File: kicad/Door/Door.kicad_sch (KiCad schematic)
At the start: 14 parts, among them Q1 Q_NMOS_GDS, Q2 Q_PMOS_GSD, SW1 SW_Push, SW2 USB/BAT, SW3 RST_BTN, U1 NODEMCU v3

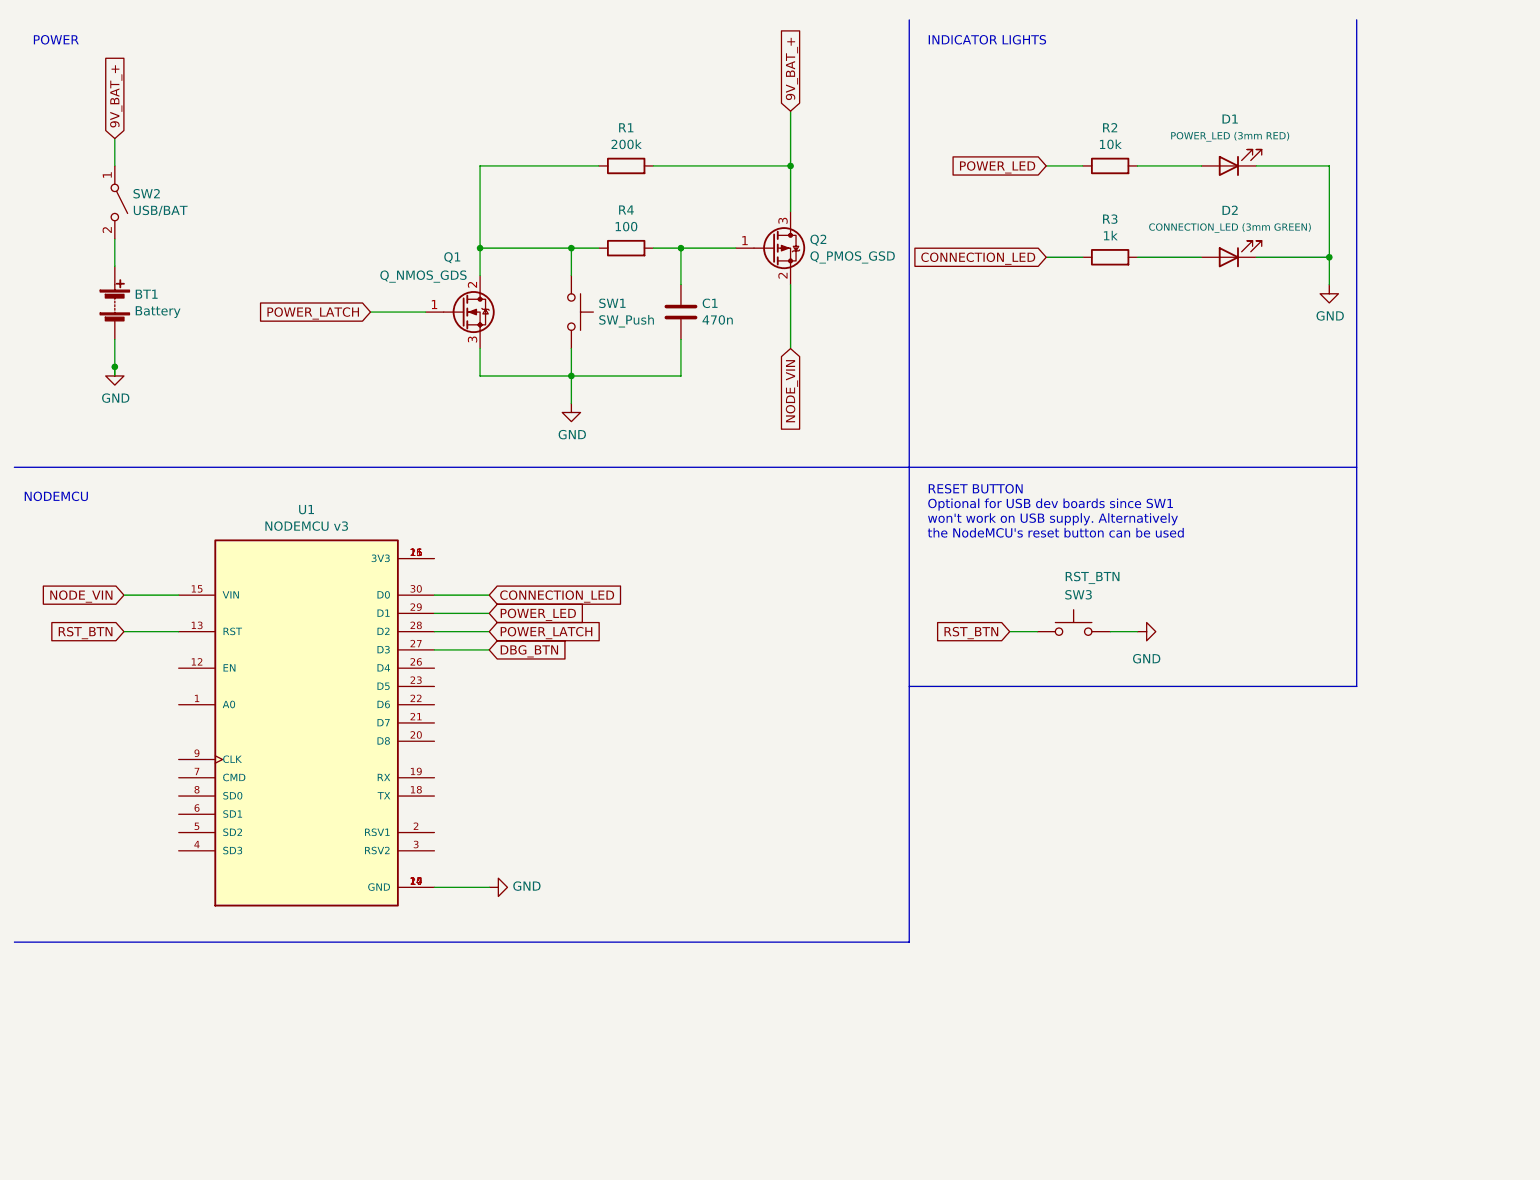
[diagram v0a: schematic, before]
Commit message: README: Added images
Signed-off-by: Patrick Pedersen <ctx.xda@gmail.com>
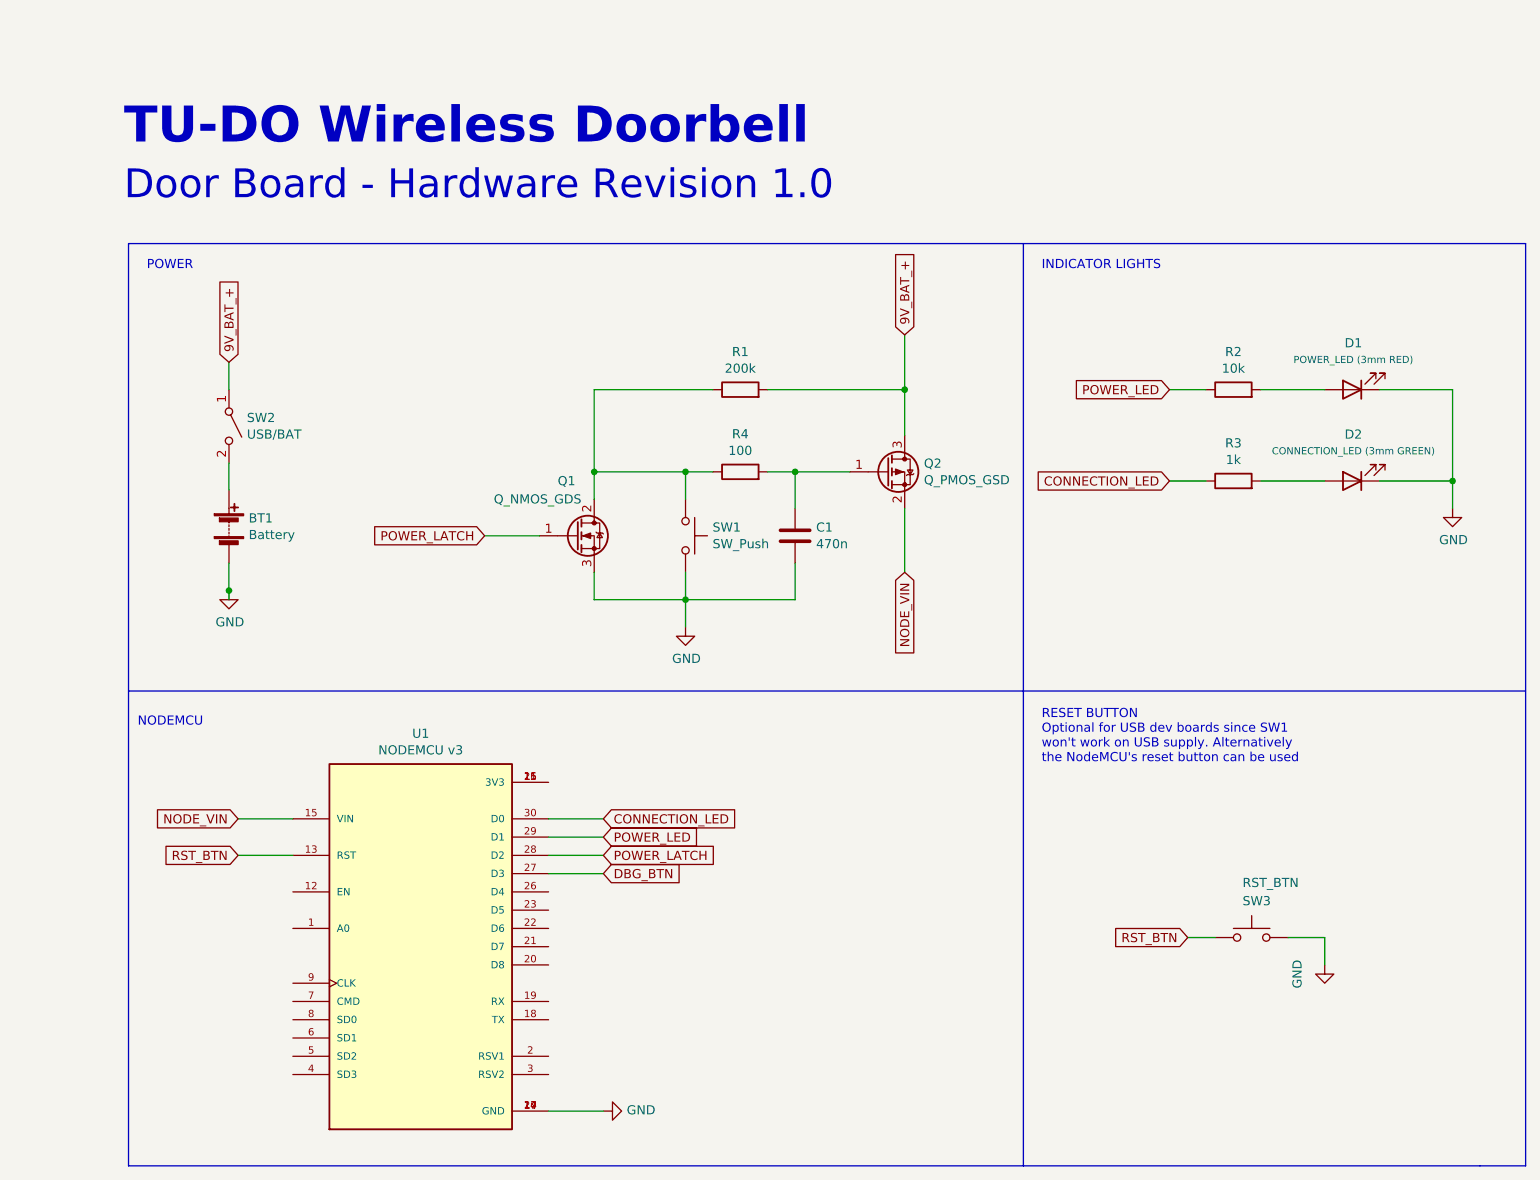
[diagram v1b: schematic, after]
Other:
- note added: "Door Board - Hardware Revision 1.0"
- note added: "TU-DO Wireless Doorbell"
- moved on the sheet: BT1, C1, D1, D2, Q1, Q2, R1, R2, R3, R4, SW1, SW2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
